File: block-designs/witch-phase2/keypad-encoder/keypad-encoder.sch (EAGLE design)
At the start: 91 parts, among them IC1 74LVC1G17DBV, IC2 74LVC1G17DBV, IC3 74LVC1G17DBV, IC4 74LVC1G17DBV, IC5 74LVC1G17DBV, IC6 74LVC1G17DBV, IC7 74LVC1G14DBV, IC8 74LVC1G14DBV

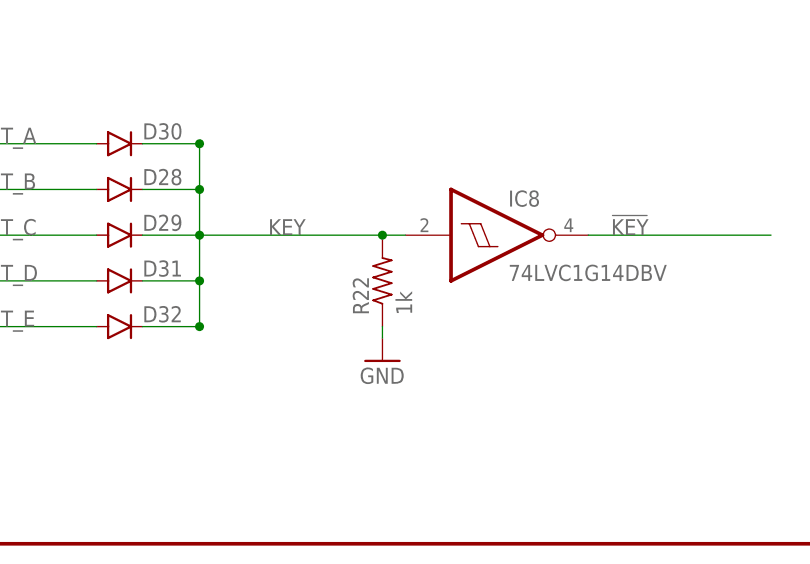
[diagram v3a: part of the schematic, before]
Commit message: change pull down from 1k to 100k
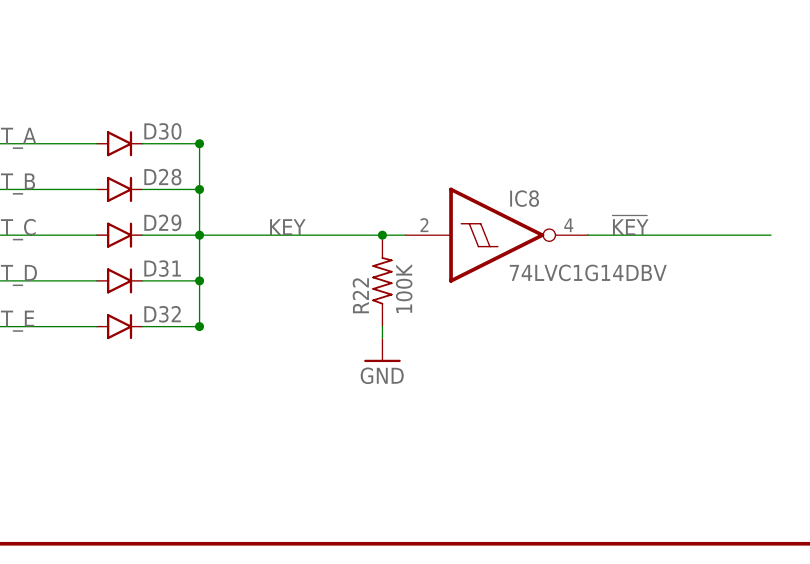
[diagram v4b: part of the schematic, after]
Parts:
- R22: value 1k -> 100K
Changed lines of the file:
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@@
 <part name="D31" library="SparkFun-DiscreteSemi" deviceset="DIODE" device="PTH"/>
 <part name="D32" library="SparkFun-DiscreteSemi" deviceset="DIODE" device="PTH"/>
-<part name="R22" library="resistor" deviceset="R-US_" device="R0805" value="1k"/>
+<part name="R22" library="resistor" deviceset="R-US_" device="R0805" value="100K"/>
 <part name="GND25" library="supply1" deviceset="GND" device=""/>
 <part name="IC8" library="74xx-little-us" deviceset="74*1G14" device="DBV" technology="LVC"/>
